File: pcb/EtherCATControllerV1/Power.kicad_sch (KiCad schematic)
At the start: 37 parts, among them U2 TPSM365R6FRDNR, U3 LDL1117S33R, U4 LP5907MFX-3.3_NOPB

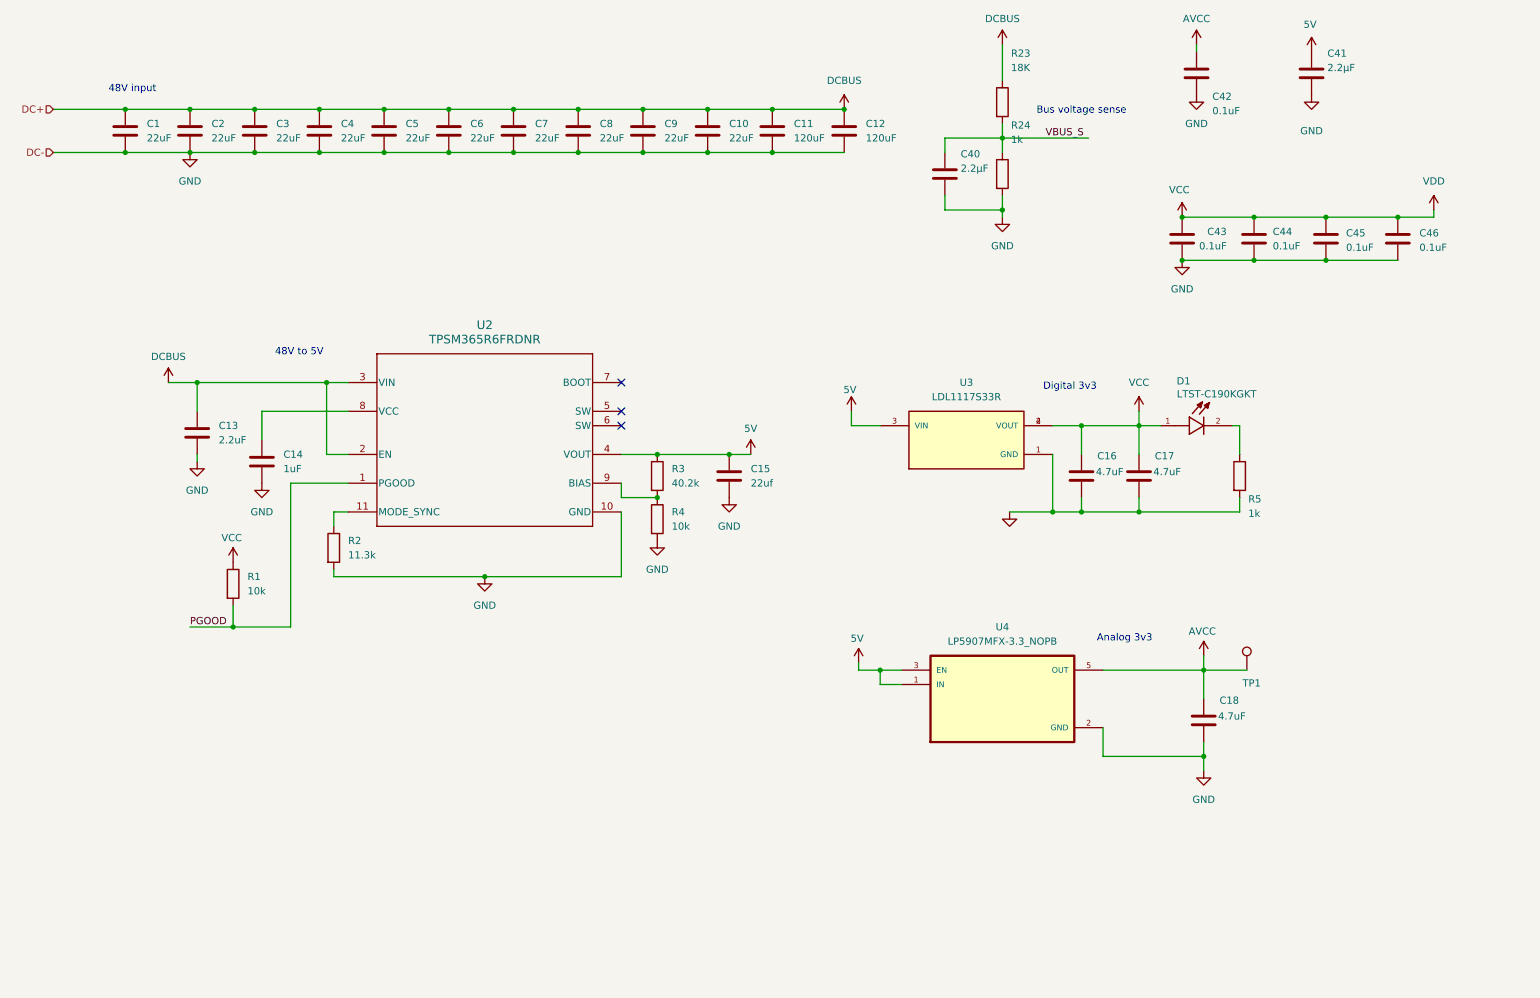
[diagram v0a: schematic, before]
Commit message: Initial design without Ethernet connectors
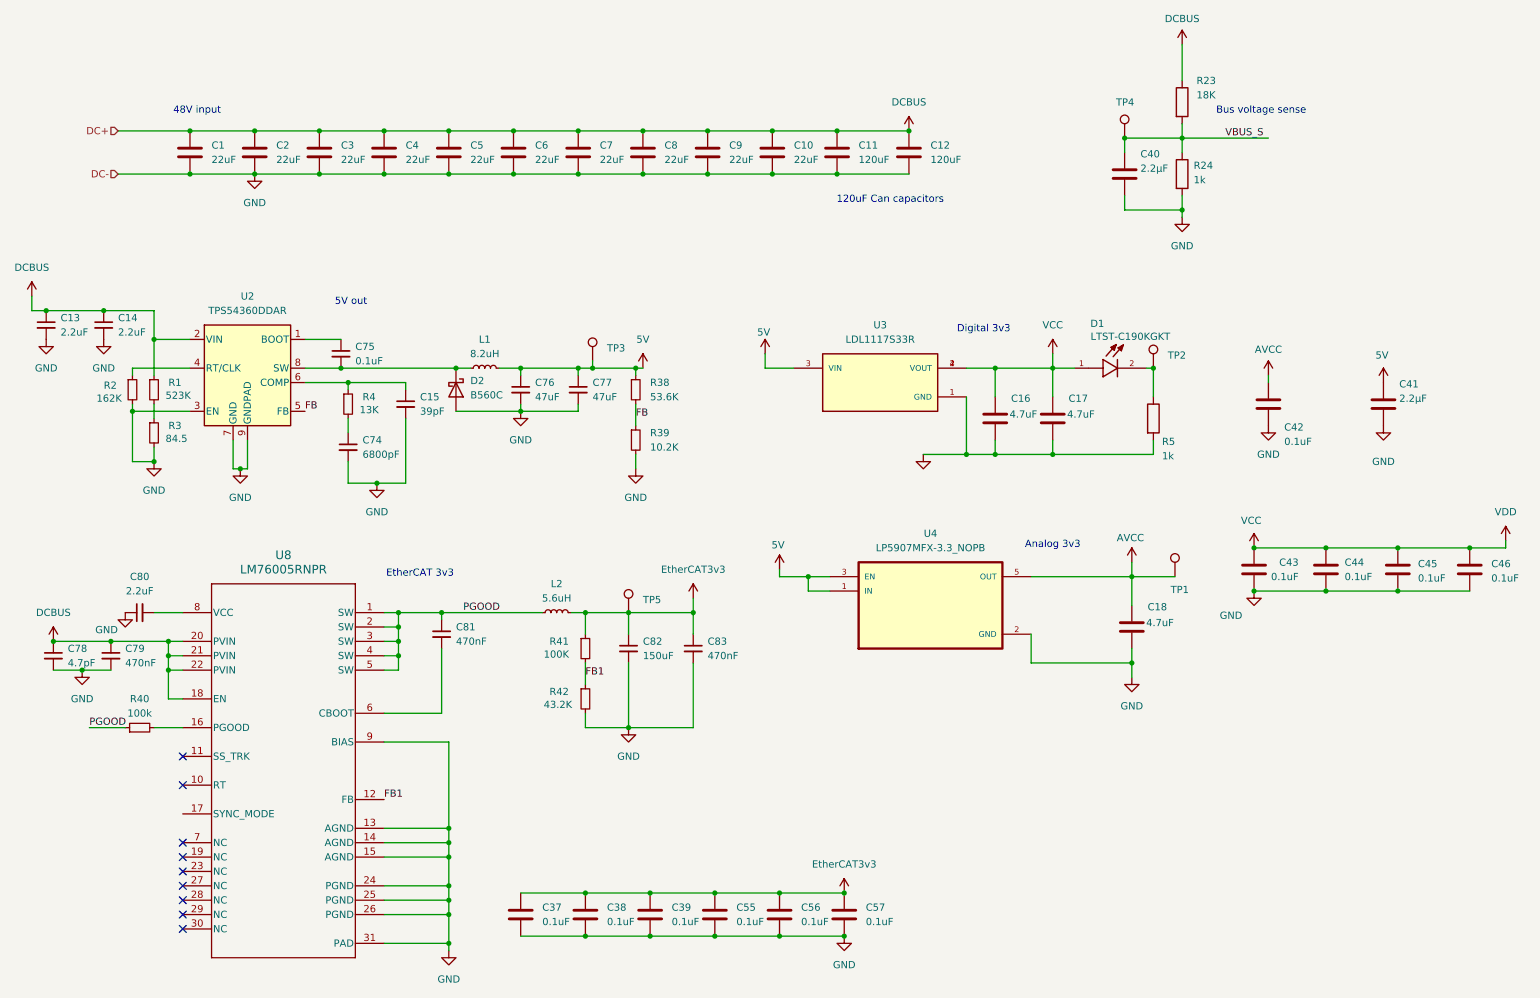
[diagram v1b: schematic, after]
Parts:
- removed C13: 2.2uF, Capacitor_SMD:C_1210_3225Metric, symbol Device:C
- removed C14: 1uF, Capacitor_SMD:C_0603_1608Metric, symbol Device:C
- removed C15: 22uf, Capacitor_SMD:C_2225_5664Metric, symbol Device:C
- removed R1, R4: 10k, Resistor_SMD:R_0603_1608Metric, symbol Device:R
- removed R2: 11.3k, Resistor_SMD:R_0603_1608Metric, symbol Device:R
- removed R3: 40.2k, Resistor_SMD:R_0603_1608Metric, symbol Device:R
- removed U2: TPSM365R6FRDNR, 5VPower:RDN0011A-MFG, symbol 2024-06-02_22-14-22:TPSM365R6FRDNR
- added C13, C14, C80: 2.2uF, symbol Device:C_Small
- added C15: 39pF, symbol Device:C_Small
- added C37, C38, C39, C55, C56, C57: 0.1uF, symbol Device:C
- added C74: 6800pF, symbol Device:C_Small
- added C75: 0.1uF, symbol Device:C_Small
- added C76, C77: 47uF, symbol Device:C_Small
- added C78: 4.7pF, symbol Device:C_Small
- added C79, C81, C83: 470nF, symbol Device:C_Small
- added C82: 150uF, symbol Device:C_Small
- added D2: B560C, symbol Device:D_Schottky
- added L1: 8.2uH, symbol Device:L_Small
- added L2: 5.6uH, symbol Device:L_Small
- added R1: 523K, symbol Device:R_Small
- added R2: 162K, symbol Device:R_Small
- added R3: 84.5, symbol Device:R_Small
- added R38: 53.6K, symbol Device:R_Small
- added R39: 10.2K, symbol Device:R_Small
- added R4: 13K, symbol Device:R_Small
- added R40: 100k, symbol Device:R_Small
- added R41: 100K, symbol Device:R_Small
- added R42: 43.2K, symbol Device:R_Small
- added TP2, TP3, TP4, TP5: TESTPOINT, TestPoint:TestPoint_Pad_1.0x1.0mm, symbol Connector:TestPoint
- added U2: TPS54360DDAR, Package_SO:TI_SO-PowerPAD-8_ThermalVias, symbol Regulator_Switching:TPS54360DDA
- added U8: LM76005RNPR, RNP0030A, symbol 2024-07-02_05-34-37:LM76005RNPR
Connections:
- net 5V: now also C76.1, C77.1, L1.2, R38.1, TP3.1
- net DCBUS: now also C13.1, C14.1, C78.1, C79.1, R1.1, U2.2 (VIN), U8.18 (EN), U8.20 (PVIN), U8.21 (PVIN), U8.22 (PVIN)
- net GND: now also C13.2, C14.2, C15.2, C37.2, C38.2, C39.2, C55.2, C56.2, C57.2, C74.2, C76.2, C77.2, C78.2, C79.2, C80.1, C82.2, C83.2, D2.2 (A), R2.2, R3.2, R39.2, R42.2, U2.3 (EN), U2.7 (GND), U2.9 (GNDPAD), U8.13 (AGND), U8.14 (AGND), U8.15 (AGND), U8.24 (PGND), U8.25 (PGND), U8.26 (PGND), U8.31 (PAD), U8.9 (BIAS)
- net PGOOD: now also C81.1, L2.1, R40.1, U8.1 (SW), U8.2 (SW), U8.3 (SW), U8.4 (SW), U8.5 (SW)
- net VBUS_S: now also TP4.1
- net at D1.2, R5.1: now also TP2.1
- new net: C15.1, R4.1, U2.6 (COMP)
- new net: C74.1, R4.2
- new net: C75.1, U2.1 (BOOT)
- new net: C75.2, D2.1 (K), L1.1, U2.8 (SW)
- new net: R2.1, U2.4 (RT/CLK)
- new net: R1.2, R3.1
- new net: R40.2, U8.16 (PGOOD)
- new net: C80.2, U8.8 (VCC)
- new net: C81.2, U8.6 (CBOOT)
- new net EtherCAT3v3: C37.1, C38.1, C39.1, C55.1, C56.1, C57.1, C82.1, C83.1, L2.2, R41.1, TP5.1
- new net FB: R38.2, R39.1, U2.5 (FB)
- new net FB1: R41.2, R42.1, U8.12 (FB)
- no-connect marks 3 -> 9
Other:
- note added: "120uF Can capacitors"
- note added: "5V out"
- note added: "EtherCAT 3v3"
- note removed: "48V to 5V"
- moved on the sheet: C1, C10, C11, C12, C16, C17, C18, C2, C3, C4, C40, C41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

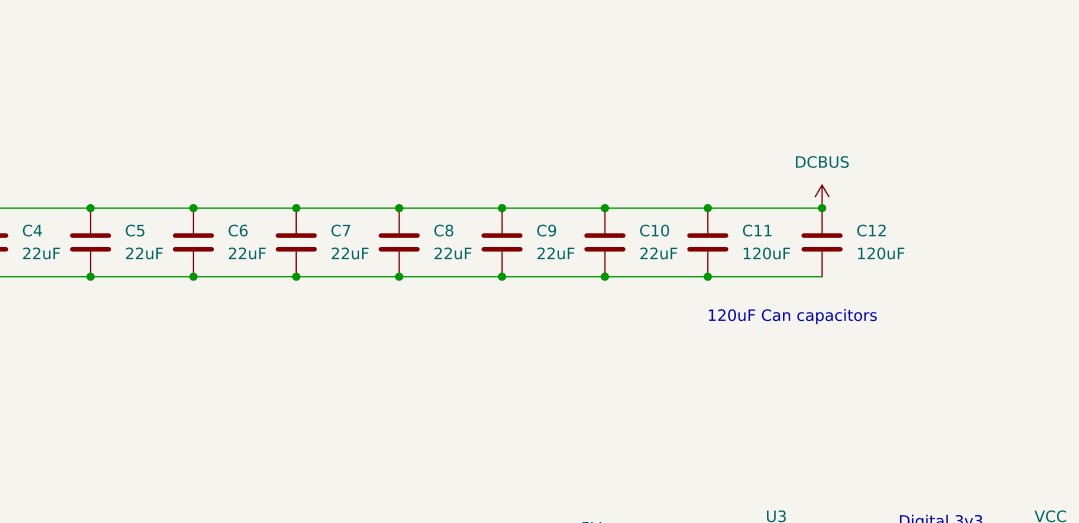
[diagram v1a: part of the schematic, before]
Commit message: Added IO Board project
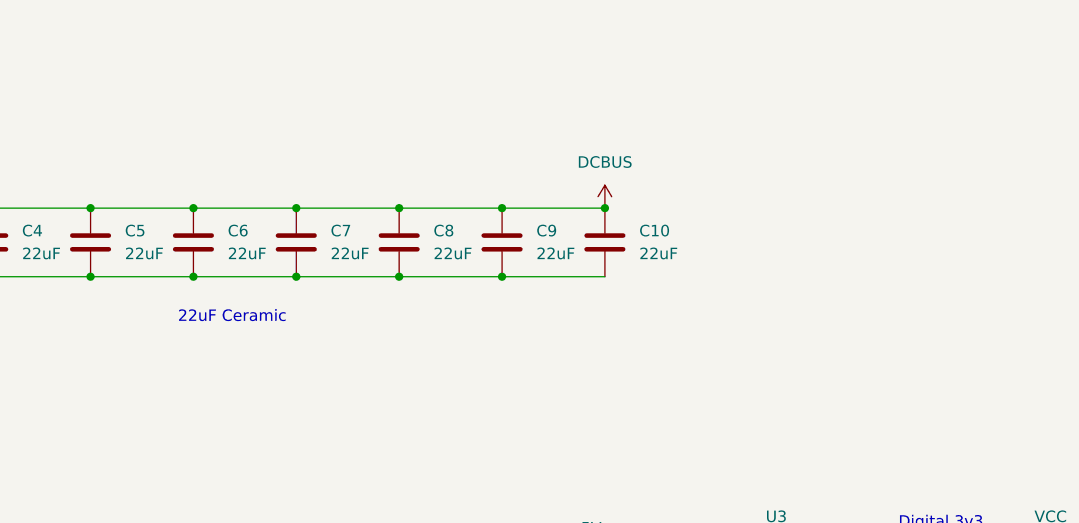
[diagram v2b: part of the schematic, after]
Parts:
- removed C11, C12: 120uF, symbol Device:C
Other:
- note added: "22uF Ceramic"
- note removed: "120uF Can capacitors"
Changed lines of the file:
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@@
 	)
 	(junction
-		(at 175.26 39.37)
-		(diameter 0)
-		(color 0 0 0 0)
-	)
-	(junction
 		(at 93.98 46.99)
 		(diameter 0)
@@
 	)
 	(junction
-		(at 162.56 39.37)
-		(diameter 0)
-		(color 0 0 0 0)
-	)
-	(junction
 		(at 223.52 40.64)
 		(diameter 0)
@@
 	)
 	(junction
-		(at 151.13 46.99)
-		(diameter 0)
-		(color 0 0 0 0)
-	)
-	(junction
 		(at 85.09 132.08)
 		(diameter 0)
@@
 	)
 	(junction
-		(at 162.56 46.99)
-		(diameter 0)
-		(color 0 0 0 0)
-	)
-	(junction
 		(at 93.98 165.1)
 		(diameter 0)
@@
 	(wire
 		(pts
-			(xy 151.13 39.37) (xy 162.56 39.37)
-		)
-		(stroke
-			(width 0)
-			(type default)
-		)
-	)
-	(wire
-		(pts
 			(xy 129.54 173.99) (xy 140.97 173.99)
 		)
@@
 	(wire
 		(pts
-			(xy 162.56 46.99) (xy 175.26 46.99)
-		)
-		(stroke
-			(width 0)
-			(type default)
-		)
-	)
-	(wire
-		(pts
 			(xy 200.66 86.36) (xy 200.66 81.28)
 		)
@@
 	(wire
 		(pts
-			(xy 151.13 46.99) (xy 162.56 46.99)
-		)
-		(stroke
-			(width 0)
-			(type default)
-		)
-	)
-	(wire
-		(pts
-			(xy 162.56 39.37) (xy 175.26 39.37)
-		)
-		(stroke
-			(width 0)
-			(type default)
-		)
-	)
-	(wire
-		(pts
 			(xy 95.25 81.28) (xy 97.79 81.28)
 		)
@@
 		)
 	)
-	(text "48V input"
+	(text "22uF Ceramic"
 		(exclude_from_sim no)
-		(at 49.53 35.814 0)
+		(at 109.728 51.562 0)
 		(effects
 			(font
@@
 		)
 	)
-	(text "120uF Can capacitors"
+	(text "48V input"
 		(exclude_from_sim no)
-		(at 171.958 51.562 0)
+		(at 49.53 35.814 0)
 		(effects
 			(font
@@
 	)
 	(symbol
+		(lib_id "power:+48V")
+		(at 151.13 39.37 0)
+		(unit 1)
+		(exclude_from_sim no)
+		(in_bom yes)
+		(on_board yes)
+		(dnp no)
+		(fields_autoplaced yes)
+		(property "Reference" "#PWR01"
+			(at 151.13 43.18 0)
+			(effects
+				(font
+					(size 1.27 1.27)
+				)
+				(hide yes)
+			)
+		)
+		(property "Value" "DCBUS"
+			(at 151.13 34.29 0)
+			(effects
+				(font
+					(size 1.27 1.27)
+				)
+			)
+		)
+		(property "Footprint" ""
+			(at 151.13 39.37 0)
+			(effects
+				(font
+					(size 1.27 1.27)
+				)
+				(hide yes)
+			)
+		)
+		(property "Datasheet" ""
+			(at 151.13 39.37 0)
+			(effects
+				(font
+					(size 1.27 1.27)
+				)
+				(hide yes)
+			)
+		)
+		(property "Description" "Power symbol creates a global label with name \"+48V\""
+			(at 151.13 39.37 0)
+			(effects
+				(font
+					(size 1.27 1.27)
+				)
+				(hide yes)
+			)
+		)
+		(pin "1"
+		)
+		(instances
+			(project "EtherCATControllerV1"
+				(path "/4c927f80-855d-490a-80b2-e5c55283621a/8ad53e1c-08f0-40db-b0fb-703203134f02"
+					(reference "#PWR01")
+					(unit 1)
+				)
+			)
+		)
+	)
+	(symbol
 		(lib_id "power:+5V")
 		(at 128.27 81.28 0)
@@
 	)
 	(symbol
-		(lib_id "Device:C")
-		(at 162.56 43.18 0)
-		(unit 1)
-		(exclude_from_sim no)
-		(in_bom yes)
-		(on_board yes)
-		(dnp no)
-		(fields_autoplaced yes)
-		(property "Reference" "C11"
-			(at 166.37 41.9099 0)
-			(effects
-				(font
-					(size 1.27 1.27)
-				)
-				(justify left)
-			)
-		)
-		(property "Value" "120uF"
-			(at 166.37 44.4499 0)
-			(effects
-				(font
-					(size 1.27 1.27)
-				)
-				(justify left)
-			)
-		)
-		(property "Footprint" ""
-			(at 163.5252 46.99 0)
-			(effects
-				(font
-					(size 1.27 1.27)
-				)
-				(hide yes)
-			)
-		)
-		(property "Datasheet" "~"
-			(at 162.56 43.18 0)
-			(effects
-				(font
-					(size 1.27 1.27)
-				)
-				(hide yes)
-			)
-		)
-		(property "Description" "Electrolytic Can Capacitor"
-			(at 162.56 43.18 0)
-			(effects
-				(font
-					(size 1.27 1.27)
-				)
-				(hide yes)
-			)
-		)
-		(property "LCSC Part Number" "C487157"
-			(at 162.56 43.18 0)
-			(effects
-				(font
-					(size 1.27 1.27)
-				)
-				(hide yes)
-			)
-		)
-		(pin "1"
-		)
-		(pin "2"
-		)
-		(instances
-			(project "EtherCATControllerV1"
-				(path "/4c927f80-855d-490a-80b2-e5c55283621a/8ad53e1c-08f0-40db-b0fb-703203134f02"
-					(reference "C11")
-					(unit 1)
-				)
-			)
-		)
-	)
-	(symbol
 		(lib_id "Device:C_Small")
 		(at 33.02 73.66 0)
@@
 	)
 	(symbol
-		(lib_id "power:+48V")
-		(at 175.26 39.37 0)
-		(unit 1)
-		(exclude_from_sim no)
-		(in_bom yes)
-		(on_board yes)
-		(dnp no)
-		(fields_autoplaced yes)
-		(property "Reference" "#PWR01"
-			(at 175.26 43.18 0)
-			(effects
-				(font
-					(size 1.27 1.27)
-				)
-				(hide yes)
-			)
-		)
-		(property "Value" "DCBUS"
-			(at 175.26 34.29 0)
-			(effects
-				(font
-					(size 1.27 1.27)
-				)
-			)
-		)
-		(property "Footprint" ""
-			(at 175.26 39.37 0)
-			(effects
-				(font
-					(size 1.27 1.27)
-				)
-				(hide yes)
-			)
-		)
-		(property "Datasheet" ""
-			(at 175.26 39.37 0)
-			(effects
-				(font
-					(size 1.27 1.27)
-				)
-				(hide yes)
-			)
-		)
-		(property "Description" "Power symbol creates a global label with name \"+48V\""
-			(at 175.26 39.37 0)
-			(effects
-				(font
-					(size 1.27 1.27)
-				)
-				(hide yes)
-			)
-		)
-		(pin "1"
-		)
-		(instances
-			(project "EtherCATControllerV1"
-				(path "/4c927f80-855d-490a-80b2-e5c55283621a/8ad53e1c-08f0-40db-b0fb-703203134f02"
-					(reference "#PWR01")
-					(unit 1)
-				)
-			)
-		)
-	)
-	(symbol
 		(lib_id "Device:C_Small")
 		(at 86.36 87.63 0)
@@
 					(unit 1)
 				)
-			)
-		)
-	)
-	(symbol
-		(lib_id "Device:C")
-		(at 175.26 43.18 0)
-		(unit 1)
-		(exclude_from_sim no)
-		(in_bom yes)
-		(on_board yes)
-		(dnp no)
-		(fields_autoplaced yes)
-		(property "Reference" "C12"
-			(at 179.07 41.9099 0)
-			(effects
-				(font
-					(size 1.27 1.27)
-				)
-				(justify left)
-			)
-		)
-		(property "Value" "120uF"
-			(at 179.07 44.4499 0)
-			(effects
-				(font
-					(size 1.27 1.27)
-				)
-				(justify left)
-			)
-		)
-		(property "Footprint" ""
-			(at 176.2252 46.99 0)
-			(effects
-				(font
-					(size 1.27 1.27)
-				)
-				(hide yes)
-			)
-		)
-		(property "Datasheet" "~"
-			(at 175.26 43.18 0)
-			(effects
-				(font
-					(size 1.27 1.27)
-				)
-				(hide yes)
-			)
-		)
-		(property "Description" "Electrolytic Can Capacitor"
-			(at 175.26 43.18 0)
-			(effects
-				(font
-					(size 1.27 1.27)
-				)
-				(hide yes)
-			)
-		)
-		(property "LCSC Part Number" "C487157"
-			(at 175.26 43.18 0)
-			(effects
-				(font
-					(size 1.27 1.27)
-				)
-				(hide yes)
-			)
-		)
-		(pin "1"
-		)
-		(pin "2"
-		)
-		(instances
-			(project "EtherCATControllerV1"
-				(path "/4c927f80-855d-490a-80b2-e5c55283621a/8ad53e1c-08f0-40db-b0fb-703203134f02"
-					(reference "C12")
-					(unit 1)
-				)
